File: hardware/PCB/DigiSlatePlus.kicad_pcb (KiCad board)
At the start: 2 copper layers, 270 x 140 mm, 126 parts, among them J1 Serial, J10 IO7, J2 USB_B, J3 +8-24 Volt, J4 Battery, J6 Mains, J7 Timecode IN, J8 Timecode OUT, J9 MISO, Q1 2N2222, Q2 2N2222, Q3 FS8205A, Q4 2N2222, SW1 RotaryEncoder-SW, SW2 1, SW3 1, SW4 1, SW5 1, SW6 BOOT, SW7 SW_DPDT_x2, U1 ESP32-S3-WROOM-1, U10 SA15-11SRWA, U11 SA15-11SRWA, U12 SA15-11SRWA, U13 SA15-11SRWA, U14 SA15-11SRWA, U15 SA15-11SRWA, U16 MAX7219, U17 SA15-11SRWA, U18 SA15-11SRWA, U19 SA15-11SRWA, U2 DS3231M, U20 SA15-11SRWA, U21 LM2596S-ADJ, U22 DW01A, U23 TP4056, U24 KA78M05_TO252, U25 LD1117S33TR_SOT223, U3 SA15-11SRWA, U4 SA15-11SRWA, U5 SA15-11SRWA, U6 SA15-11SRWA, U7 MAX7219, U8 SA15-11SRWA, U9 SA15-11SRWA

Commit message: bugfixes in board
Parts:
- added D8: 1N4148, Diode_SMD:D_PowerDI-123, B.Cu at (290.1, 149.0)
- added JP1: charge, Jumper:SolderJumper-2_P1.3mm_Open_TrianglePad1.0x1.5mm, B.Cu at (295.7, 149.0)
- added OHW-Logo: LOGO, Logos:Open-Source-Hardware-Logo, B.Cu at (119.0, 94.0)
- added R14: 220R, Resistor_SMD:R_1206_3216Metric, B.Cu at (290.5, 144.0)
- J3: moved to B.Cu
- turned J3 to -90 degrees
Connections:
- C1 pad 1: +3.3V -> VCC-INT
- C19 pad 1: +3.3V -> VCC-INT
- C2 pad 1: +3.3V -> VCC-INT
- C20 pad 1: +3.3V -> VCC-INT
- J1 pad 4: +3.3V -> VCC-INT
- R1 pad 1: +3.3V -> VCC-INT
- R2 pad 1: +3.3V -> VCC-INT
- R25 pad 1: +3.3V -> VCC-INT
- R26 pad 1: +3.3V -> VCC-INT
- R27 pad 1: +3.3V -> VCC-INT
- R28 pad 1: +3.3V -> VCC-INT
- R29 pad 1: +3.3V -> VCC-INT
- R3 pad 1: +3.3V -> VCC-INT
- R30 pad 1: +3.3V -> VCC-INT
- R31 pad 1: +3.3V -> VCC-INT
- R4 pad 1: +3.3V -> VCC-INT
- R5 pad 1: +3.3V -> VCC-INT
- R6 pad 1: +3.3V -> VCC-INT
- R7 pad 1: +3.3V -> VCC-INT
- SW1 pad SH: (no net) -> GND
- U1 pad 2: +3.3V -> VCC-INT
- U2 pad 2: +3.3V -> VCC-INT
- U25 pad 2: +3.3V -> VCC-INT
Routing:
- net GND: track 941.0 -> 111.8 mm, vias 5 -> 38
- net VCC-INT: track 81.9 -> 592.1 mm, vias 0 -> 1
- net +3.3V: track 484.1 -> 0.00 mm, vias 5 -> 0
- net +5V: track 552.1 -> 624.2 mm, vias 3 -> 5
- net SC-D: track 293.8 -> 262.2 mm, vias 0 -> 1
- net SC-8: track 117.6 -> 99.8 mm
- net SW2: track 233.2 -> 216.2 mm
- net TC-OUT: track 191.8 -> 175.0 mm, vias 1 -> 3
- net F: track 263.1 -> 277.1 mm
- net SW4: track 258.1 -> 271.8 mm
- net Net-(U21-VIN): track 87.7 -> 98.7 mm, vias 1 -> 0
- net DOTS: track 44.0 -> 54.4 mm
- net SC-G: track 249.8 -> 240.6 mm, vias 0 -> 1
- net B: track 262.7 -> 253.5 mm
- net SCK: track 166.2 -> 157.1 mm
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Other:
- board text added: "12V"
- board text added: "BATT 3.7V"
- board text added: "LCD contrast"
- board text added: "ON"
- board text added: "TC-IN"
- board text added: "TC-OUT"
- board text added: "USB"
- board text added: "chrg"
- board text added: "clap switch"
- board text added: "scene/take brightnes"
- board text added: "serial"
- board text added: "timecode brightnes"

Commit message: dot matrix bugfixes
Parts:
- removed Hole1, Hole2, Hole3, Hole4, Hole5, Hole6: MountingHole_3.2mm_M3_Pad, MountingHole:MountingHole_3.2mm_M3_Pad
- removed REF**: KiCad-Logo2_6mm_SilkScreen, Symbol:KiCad-Logo2_6mm_SilkScreen
- added 1: MountingHole_3.2mm_M3_DIN965_Pad, MountingHole:MountingHole_3.2mm_M3_DIN965_Pad, F.Cu at (76.0, 70.0)
- added 2: MountingHole_3.2mm_M3_DIN965_Pad, MountingHole:MountingHole_3.2mm_M3_DIN965_Pad, F.Cu at (207.0, 70.0)
- added 3: MountingHole_3.2mm_M3_DIN965_Pad, MountingHole:MountingHole_3.2mm_M3_DIN965_Pad, F.Cu at (338.0, 70.0)
- added 4: MountingHole_3.2mm_M3_DIN965_Pad, MountingHole:MountingHole_3.2mm_M3_DIN965_Pad, F.Cu at (76.0, 202.0)
- added 5: MountingHole_3.2mm_M3_DIN965_Pad, MountingHole:MountingHole_3.2mm_M3_DIN965_Pad, F.Cu at (207.0, 202.0)
- added 6: MountingHole_3.2mm_M3_DIN965_Pad, MountingHole:MountingHole_3.2mm_M3_DIN965_Pad, F.Cu at (338.0, 202.0)
- added C22: 100nF/50V, Capacitor_SMD:C_1206_3216Metric_Pad1.33x1.80mm_HandSolder, B.Cu at (116.8, 135.8)
- added C23: 470uF/10V, Capacitor_Tantalum_SMD:CP_EIA-7343-31_Kemet-D_Pad2.25x2.55mm_HandSolder, B.Cu at (137.8, 136.1)
- added C24: 100nF/50V, Capacitor_SMD:C_1206_3216Metric_Pad1.33x1.80mm_HandSolder, B.Cu at (147.9, 136.5)
- added C25: 470uF/10V, Capacitor_Tantalum_SMD:CP_EIA-7343-31_Kemet-D_Pad2.25x2.55mm_HandSolder, B.Cu at (168.9, 136.8)
- added C26: 100nF/50V, Capacitor_SMD:C_1206_3216Metric_Pad1.33x1.80mm_HandSolder, B.Cu at (180.3, 135.9)
- added C27: 470uF/10V, Capacitor_Tantalum_SMD:CP_EIA-7343-31_Kemet-D_Pad2.25x2.55mm_HandSolder, B.Cu at (202.5, 136.2)
- added C28: 100nF/50V, Capacitor_SMD:C_1206_3216Metric_Pad1.33x1.80mm_HandSolder, B.Cu at (212.7, 135.2)
- added C29: 470uF/10V, Capacitor_Tantalum_SMD:CP_EIA-7343-31_Kemet-D_Pad2.25x2.55mm_HandSolder, B.Cu at (233.7, 135.8)
- added C30: 100nF/50V, Capacitor_SMD:C_1206_3216Metric_Pad1.33x1.80mm_HandSolder, B.Cu at (244.3, 136.2)
- added C31: 470uF/10V, Capacitor_Tantalum_SMD:CP_EIA-7343-31_Kemet-D_Pad2.25x2.55mm_HandSolder, B.Cu at (265.3, 136.7)
- added C32: 100nF/50V, Capacitor_SMD:C_1206_3216Metric_Pad1.33x1.80mm_HandSolder, B.Cu at (276.4, 136.2)
- added C33: 470uF/10V, Capacitor_Tantalum_SMD:CP_EIA-7343-31_Kemet-D_Pad2.25x2.55mm_HandSolder, B.Cu at (297.4, 135.8)
- added C34: 100nF/50V, Capacitor_SMD:C_1206_3216Metric_Pad1.33x1.80mm_HandSolder, B.Cu at (308.8, 135.9)
- added C35: 470uF/10V, Capacitor_Tantalum_SMD:CP_EIA-7343-31_Kemet-D_Pad2.25x2.55mm_HandSolder, B.Cu at (329.8, 136.6)
- added U26: ~, FMY-12883:FMY-12883, F.Cu at (94.4, 136.0)
- added U27: MAX7219, Package_SO:SOIC-24W_7.5x15.4mm_P1.27mm, B.Cu at (254.3, 136.0)
- added U28: ~, FMY-12883:FMY-12883, F.Cu at (254.3, 136.0)
- added U29: MAX7219, Package_SO:SOIC-24W_7.5x15.4mm_P1.27mm, B.Cu at (286.4, 136.0)
- added U30: ~, FMY-12883:FMY-12883, F.Cu at (286.4, 136.0)
- added U31: MAX7219, Package_SO:SOIC-24W_7.5x15.4mm_P1.27mm, B.Cu at (318.4, 136.0)
- added U32: ~, FMY-12883:FMY-12883, F.Cu at (318.4, 136.0)
- C2, D8, JP1, R14, R5, R6, R7, U2: moved to F.Cu
- U10, U3, U4, U6: value SA15-11SRWA -> MAX7219; footprint 7-segment-led:FYS-12011A -> Package_SO:SOIC-24W_7.5x15.4mm_P1.27mm; moved to B.Cu
- U11, U5, U8, U9: value SA15-11SRWA -> ~; footprint 7-segment-led:FYS-12011A -> FMY-12883:FMY-12883
- moved C4 155.4 mm to (85.1, 135.8), turned to 90 degrees
- moved R15 148.1 mm to (224.0, 157.0), turned to 180 degrees
- moved R16 141.2 mm to (222.7, 162.8), turned to 90 degrees
- moved R13 141.2 mm to (217.3, 157.0), turned to 180 degrees
- moved Q2 136.4 mm to (217.5, 163.0), turned to 0 degrees
- moved C5 129.1 mm to (105.4, 136.1), turned to 90 degrees
- moved D7 126.7 mm to (205.0, 160.0), turned to 0 degrees
- moved RV2 105.7 mm to (313.9, 156.3), turned to 180 degrees
- moved U11 90.0 mm to (222.5, 136.0)
- moved U8 63.7 mm to (158.4, 136.0)
- moved U2 63.5 mm to (287.8, 197.5)
- moved U9 61.8 mm to (190.4, 136.0)
- moved R6 60.8 mm to (298.4, 196.2)
- moved U10 59.9 mm to (222.5, 136.0), turned to -90 degrees
- moved R7 57.5 mm to (278.2, 194.4), turned to -90 degrees
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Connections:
- C1 pad 1: VCC-INT -> +3.3V
- C19 pad 1: VCC-INT -> +3.3V
- C2 pad 1: VCC-INT -> +3.3V
- C20 pad 1: VCC-INT -> +3.3V
- J1 pad 4: VCC-INT -> +3.3V
- R1 pad 1: VCC-INT -> +3.3V
- R14 pad 1: VCC-INT -> +3.3V
- R2 pad 1: VCC-INT -> +3.3V
- R25 pad 1: VCC-INT -> +3.3V
- R26 pad 1: VCC-INT -> +3.3V
- R27 pad 1: VCC-INT -> +3.3V
- R28 pad 1: VCC-INT -> +3.3V
- R29 pad 1: VCC-INT -> +3.3V
- R3 pad 1: VCC-INT -> +3.3V
- R30 pad 1: VCC-INT -> +3.3V
- R31 pad 1: VCC-INT -> +3.3V
- R4 pad 1: VCC-INT -> +3.3V
- R5 pad 1: VCC-INT -> +3.3V
- R6 pad 1: VCC-INT -> +3.3V
- R7 pad 1: VCC-INT -> +3.3V
- RV2 pad 1: Net-(U7-ISET) -> LED-BN
- RV2 pad 2: Net-(U7-ISET) -> LED-BN
- SW1 pad SH: GND -> (no net)
- U1 pad 2: VCC-INT -> +3.3V
- U10 pad 1: SC-7 -> Net-(U10-DIN)
- U10 pad 10: SC-G -> C6-4
- U10 pad 2: SC-E -> C1-4
- U10 pad 3: SC-D -> C5-4
- U10 pad 4: SC-C -> GND
- U10 pad 5: SC-7 -> C7-4
- U10 pad 6: SC-B -> C3-4
- U10 pad 7: SC-A -> C4-4
- U10 pad 8: SC-DP -> C8-4
- U10 pad 9: SC-F -> GND
- U11 pad 1: SC-8 -> R5-4
- U11 pad 10: SC-G -> C4-4
- U11 pad 2: SC-E -> R7-4
- U11 pad 3: SC-D -> C2-4
- U11 pad 4: SC-C -> C3-4
- U11 pad 5: SC-8 -> R8-4
- U11 pad 6: SC-B -> C5-4
- U11 pad 7: SC-A -> R6-4
- U11 pad 8: SC-DP -> R3-4
- U11 pad 9: SC-F -> R1-4
- U2 pad 2: VCC-INT -> +3.3V
- U25 pad 2: VCC-INT -> +3.3V
- U3 pad 1: SC-1 -> Net-(U3-DIN)
- U3 pad 10: SC-G -> C6-8
- U3 pad 2: SC-E -> C1-8
- U3 pad 3: SC-D -> C5-8
- U3 pad 4: SC-C -> GND
- U3 pad 5: SC-1 -> C7-8
- U3 pad 6: SC-B -> C3-8
- U3 pad 7: SC-A -> C4-8
- U3 pad 8: SC-DP -> C8-8
- U3 pad 9: SC-F -> GND
- U4 pad 1: SC-2 -> Net-(U4-DIN)
- U4 pad 10: SC-G -> C6-7
- U4 pad 2: SC-E -> C1-7
- U4 pad 3: SC-D -> C5-7
- U4 pad 4: SC-C -> GND
- U4 pad 5: SC-2 -> C7-7
- U4 pad 6: SC-B -> C3-7
- U4 pad 7: SC-A -> C4-7
- U4 pad 8: SC-DP -> C8-7
- U4 pad 9: SC-F -> GND
- U5 pad 1: SC-3 -> R5-7
- U5 pad 10: SC-G -> C4-7
- U5 pad 2: SC-E -> R7-7
- U5 pad 3: SC-D -> C2-7
- U5 pad 4: SC-C -> C3-7
- U5 pad 5: SC-3 -> R8-7
- U5 pad 6: SC-B -> C5-7
- U5 pad 7: SC-A -> R6-7
- U5 pad 8: SC-DP -> R3-7
- U5 pad 9: SC-F -> R1-7
- U6 pad 1: SC-4 -> Net-(U6-DIN)
- U6 pad 10: SC-G -> C6-6
- U6 pad 2: SC-E -> C1-6
- U6 pad 3: SC-D -> C5-6
- U6 pad 4: SC-C -> Net-(C24-Pad2)
- U6 pad 5: SC-4 -> C7-6
- U6 pad 6: SC-B -> C3-6
- U6 pad 7: SC-A -> C4-6
- U6 pad 8: SC-DP -> C8-6
- U6 pad 9: SC-F -> Net-(C24-Pad2)
- U7 pad 1: MOSI -> DO4-DI5
- U7 pad 10: SC-6 -> C6-5
- U7 pad 11: SC-2 -> C2-5
- U7 pad 12: LOAD-SC -> LOAD-1
- U7 pad 14: SC-A -> R1-5
- U7 pad 15: SC-F -> R6-5
- U7 pad 16: SC-B -> R2-5
- U7 pad 17: SC-G -> R7-5
- U7 pad 18: Net-(U7-ISET) -> LED-BN
- U7 pad 2: SC-1 -> C1-5
- U7 pad 20: SC-C -> R3-5
- U7 pad 21: SC-E -> R5-5
- U7 pad 22: SC-DP -> R8-5
- U7 pad 23: SC-D -> R4-5
- U7 pad 24: unconnected-(U7-DOUT-Pad24) -> Net-(U6-DIN)
- U7 pad 3: SC-5 -> C5-5
- U7 pad 4: GND -> Net-(C26-Pad2)
- U7 pad 5: SC-7 -> C7-5
- U7 pad 6: SC-3 -> C3-5
- U7 pad 7: SC-4 -> C4-5
- U7 pad 8: SC-8 -> C8-5
- U7 pad 9: GND -> Net-(C26-Pad2)
- U8 pad 1: SC-5 -> R5-6
- U8 pad 10: SC-G -> C4-6
- U8 pad 2: SC-E -> R7-6
- U8 pad 3: SC-D -> C2-6
- U8 pad 4: SC-C -> C3-6
- U8 pad 5: SC-5 -> R8-7
- U8 pad 6: SC-B -> C5-6
- U8 pad 7: SC-A -> R6-6
- U8 pad 8: SC-DP -> R3-6
- U8 pad 9: SC-F -> R1-6
- U9 pad 1: SC-6 -> R5-5
- U9 pad 10: SC-G -> C4-5
- U9 pad 2: SC-E -> R7-5
- U9 pad 3: SC-D -> C2-5
- U9 pad 4: SC-C -> C3-5
- U9 pad 5: SC-6 -> R8-5
- U9 pad 6: SC-B -> C5-5
- U9 pad 7: SC-A -> R6-5
- U9 pad 8: SC-DP -> R3-5
- U9 pad 9: SC-F -> R1-5
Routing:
- net +5V: track 624.2 -> 0.00 mm, vias 5 -> 0
- net VCC-INT: track 592.1 -> 0.00 mm, vias 1 -> 0
- net F: track 277.1 -> 0.00 mm
- net C: track 276.9 -> 0.00 mm
- net E: track 274.0 -> 0.00 mm, vias 1 -> 0
- net SW4: track 271.8 -> 0.00 mm, vias 1 -> 0
- net ROT-CLK: track 271.0 -> 0.00 mm, vias 1 -> 0
- net ROT-DT: track 270.0 -> 0.00 mm, vias 1 -> 0
- net D: track 268.9 -> 0.00 mm
- net ROT-SW: track 265.5 -> 0.00 mm, vias 2 -> 0
- net SC-D: track 262.2 -> 0.00 mm, vias 1 -> 0
- net A: track 261.5 -> 0.00 mm
- net G: track 261.0 -> 0.00 mm, vias 4 -> 0
- net SC-C: track 259.5 -> 0.00 mm, vias 3 -> 0
- net SC-E: track 259.0 -> 0.00 mm
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
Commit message: added KiCad libraries schematic bugfixes
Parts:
- BT1: footprint Battery:BatteryHolder_ComfortableElectronic_CH273-2450_1x2450 -> battery holder:BatteryHolder_ComfortableElectronic_CH273-2450_1x2450
- C2, D8, JP1, R14, R7, U2: moved to B.Cu
- SW1: footprint Rotary_Encoder:RotaryEncoder_Bourns_Horizontal_PEC12R-2x17F-Sxxxx -> rotary:RotaryEncoder_Bourns_Horizontal
- moved R7 97.9 mm to (302.0, 99.5)
- moved R14 95.6 mm to (302.5, 93.5), turned to 0 degrees
- moved U2 95.6 mm to (293.4, 102.1), turned to 180 degrees
- moved D8 94.1 mm to (302.0, 90.0), turned to 0 degrees
- moved C2 94.1 mm to (296.1, 94.0), turned to 180 degrees
- moved JP1 92.7 mm to (296.4, 90.0), turned to 180 degrees
- moved Q1 17.5 mm to (269.8, 114.1)
- moved R11 17.5 mm to (278.5, 114.0)
- moved R12 17.5 mm to (274.2, 114.0)
- moved C3 2.00 mm to (294.4, 176.0)
- moved U1 2.00 mm to (327.7, 95.2)
- moved BT1 2.00 mm to (304.5, 176.0)
- moved C1 1.80 mm to (332.4, 118.4)
- moved J10 1.80 mm to (324.2, 117.4)
- moved R1 1.80 mm to (329.0, 118.3)
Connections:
- net Net-(U21-VIN) renamed +12V
- U1 pad 23: LOAD -> LOAD-TC
- U1 pad 26: LOAD-SC -> LOAD-2
- U1 pad 35: LOAD -> LOAD-1
- U10 pad 24: DO4-DI5 -> unconnected-(U10-DOUT-Pad24)
- U16 pad 12: LOAD -> LOAD-TC
- U4 pad 12: LOAD-1 -> LOAD-2
- U6 pad 12: LOAD-1 -> LOAD-2
- U7 pad 1: DO4-DI5 -> MOSI
- U7 pad 12: LOAD-1 -> LOAD-2

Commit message: first 1.0 board version
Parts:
- J2: footprint Connector_USB:USB_B_Lumberg_2411_02_Horizontal -> USB-B:USB_B_Lumberg_2411_02_Horizontal
- J3: footprint Connector_BarrelJack:BarrelJack_GCT_DCJ200-10-A_Horizontal -> barrel jack:DC_Power_Jack_PCB_Mounted_2.1mm
- moved HOLE-3 10.0 mm to (328.0, 70.0)
- turned J3 to 180 degrees
- renumbered 1 to HOLE-1, 2 to HOLE-2, 3 to HOLE-3, 4 to HOLE-4, 5 to HOLE-5, 6 to HOLE-6
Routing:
- net +5V: track 0.00 -> 780.5 mm, vias 0 -> 2
- net +3.3V: track 0.00 -> 537.0 mm, vias 0 -> 2
- net GND: track 0.00 -> 445.9 mm, vias 0 -> 72
- net SCK: track 0.00 -> 402.9 mm, vias 0 -> 11
- net SW4: track 0.00 -> 334.1 mm, vias 0 -> 1
- net ROT-SW: track 0.00 -> 322.5 mm, vias 0 -> 1
- net ROT-DT: track 0.00 -> 311.5 mm, vias 0 -> 1
- net DP: track 0.00 -> 300.2 mm, vias 0 -> 4
- net SW3: track 0.00 -> 292.2 mm, vias 0 -> 2
- net ROT-CLK: track 0.00 -> 291.1 mm, vias 0 -> 2
- net C: track 0.00 -> 281.4 mm, vias 0 -> 4
- net D: track 0.00 -> 274.4 mm, vias 0 -> 1
- net G: track 0.00 -> 272.1 mm, vias 0 -> 3
- net D5: track 0.00 -> 271.0 mm, vias 0 -> 3
- net A: track 0.00 -> 268.8 mm
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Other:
- board text added: "clap sw"
- board text removed: "clap switch"

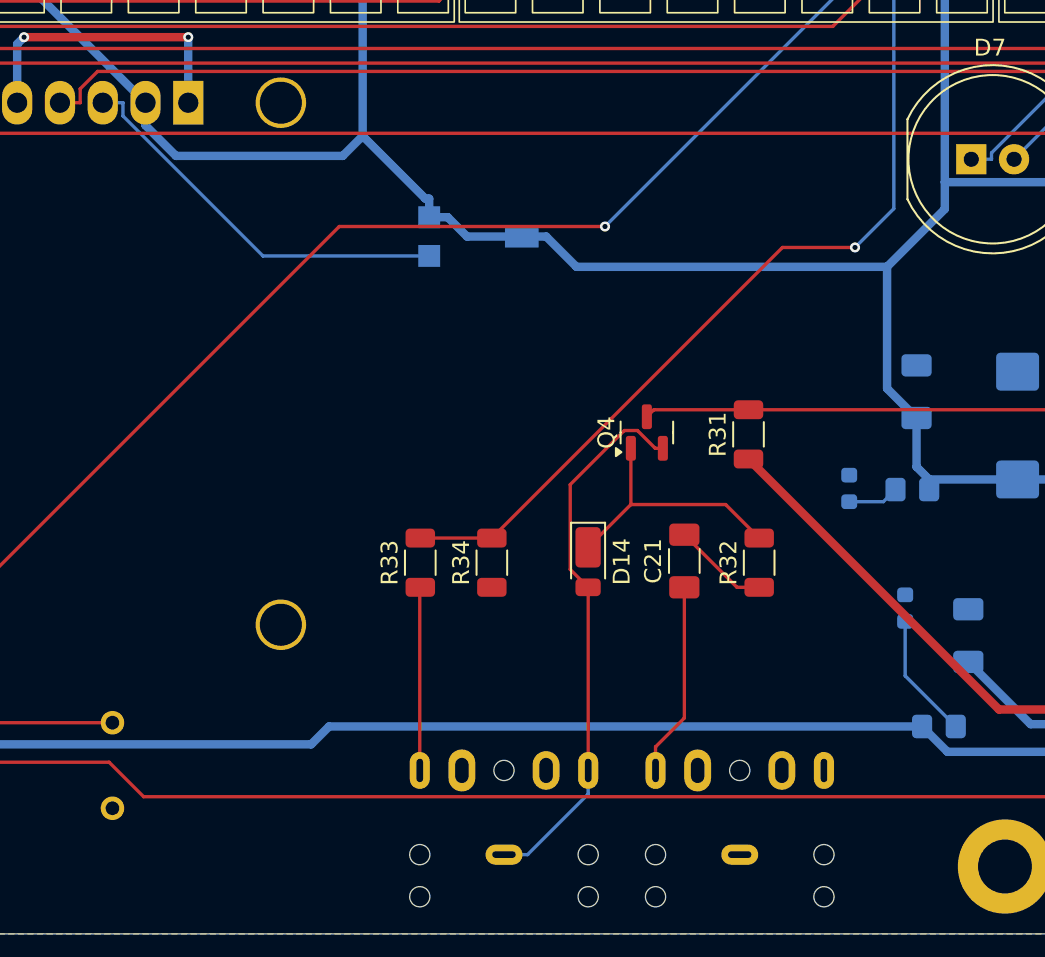
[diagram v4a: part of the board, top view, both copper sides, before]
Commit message: minor bugfixes in schematics and board
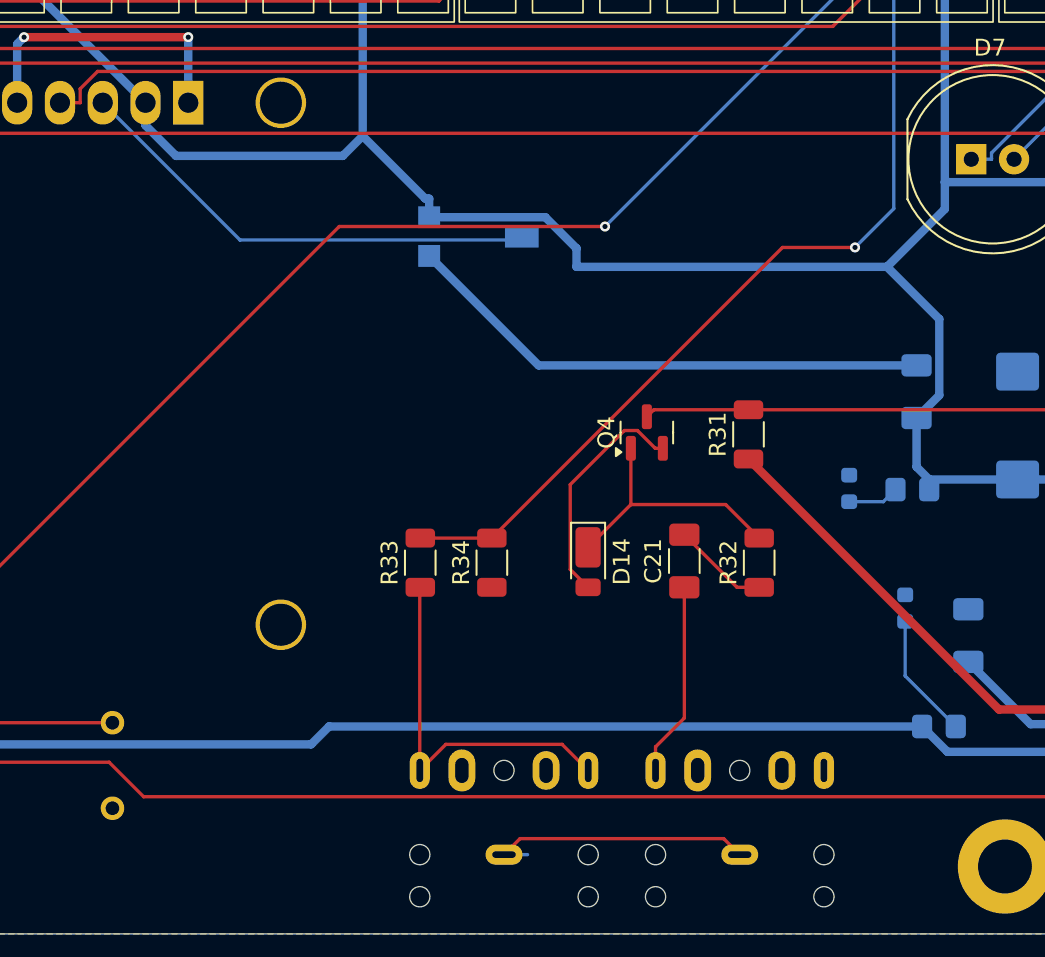
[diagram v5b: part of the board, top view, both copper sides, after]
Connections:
- D14 pad 2: Net-(D14-A) -> GND
- J8 pad R: Net-(D14-A) -> Net-(J8-PadR)
- J8 pad S: Net-(D14-A) -> GND
- J8 pad T: Net-(J8-PadT) -> Net-(J8-PadR)
- Q4 pad 2: Net-(D14-A) -> GND
- R33 pad 1: Net-(J8-PadT) -> Net-(J8-PadR)
- RV1 pad 2: +5V -> Net-(DS1-VO)
- RV1 pad 3: Net-(DS1-VO) -> GND
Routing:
- net GND: track 445.9 -> 507.5 mm
- net Net-(D14-A): track 32.6 -> 0.00 mm
- net Net-(J8-PadR): track 0.00 -> 22.2 mm
- net Net-(J8-PadT): track 10.9 -> 0.00 mm
- net Net-(DS1-VO): track 23.6 -> 28.4 mm
- net +5V: track 780.5 -> 782.3 mm
